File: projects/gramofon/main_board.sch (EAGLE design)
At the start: 25 parts

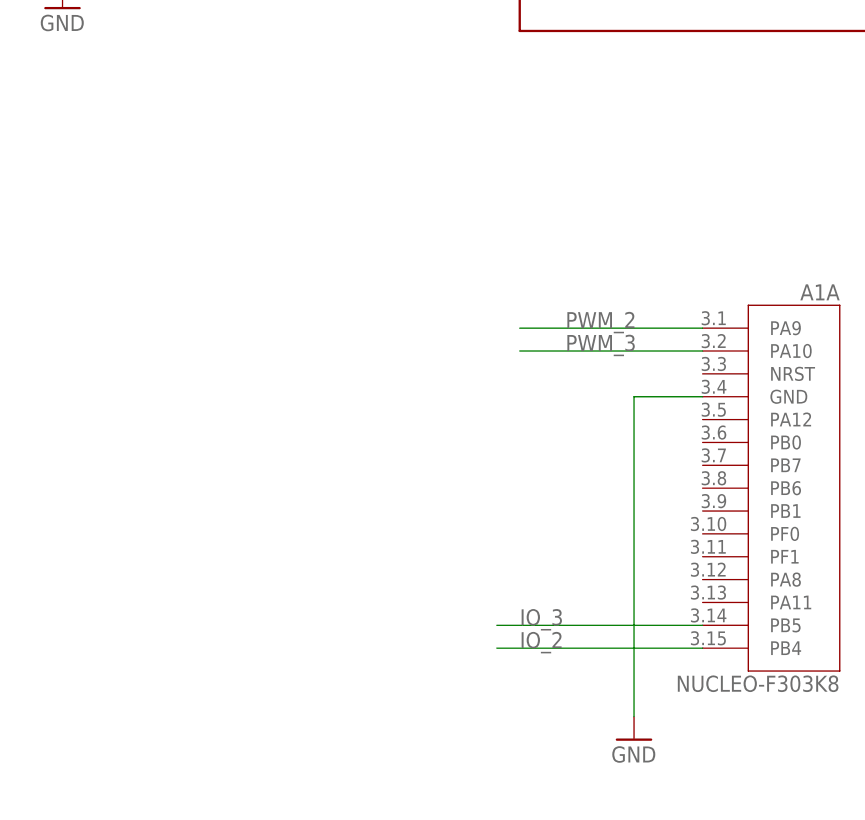
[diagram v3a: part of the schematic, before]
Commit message: updated battery board
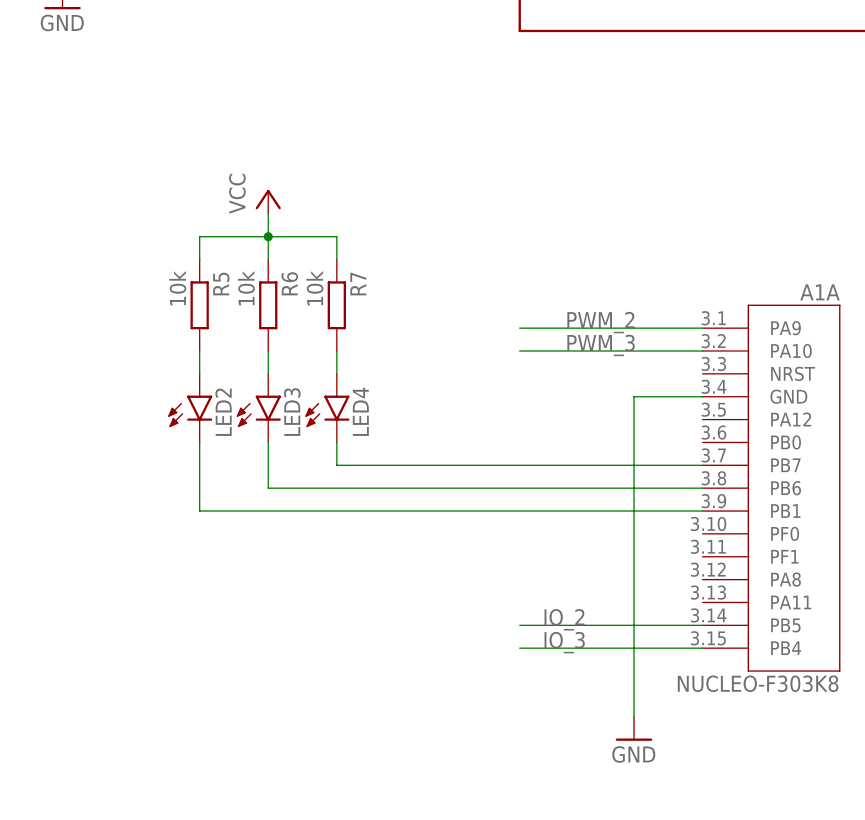
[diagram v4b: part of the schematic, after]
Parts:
- added LED2, LED3, LED4: (no value), led:LEDCHIPLED_1206
- added R5, R6, R7: 10k, rcl:R-EU_R1206
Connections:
- new net N$11: LED4.A, R7.2
- new net N$12: LED3.A, R6.2
- new net N$13: LED2.A, R5.2
- new net N$2: A1A.PB1, LED2.C
- new net N$3: A1A.PB6, LED3.C
- new net N$4: A1A.PB7, LED4.C
- net IO_2: now also A1A.PB5; no longer A1A.PB4
- net IO_3: now also A1A.PB4; no longer A1A.PB5
- net VCC: now also R5.1, R6.1, R7.1
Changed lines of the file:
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@@
 <part name="X10" library="con-wago-500" library_urn="urn:adsk.eagle:library:195" deviceset="W237-102" device="" package3d_urn="urn:adsk.eagle:package:10688/1"/>
 <part name="X11" library="con-wago-500" library_urn="urn:adsk.eagle:library:195" deviceset="W237-102" device="" package3d_urn="urn:adsk.eagle:package:10688/1"/>
+<part name="LED2" library="led" library_urn="urn:adsk.eagle:library:259" deviceset="LED" device="CHIPLED_1206" package3d_urn="urn:adsk.eagle:package:15823/2"/>
+<part name="LED3" library="led" library_urn="urn:adsk.eagle:library:259" deviceset="LED" device="CHIPLED_1206" package3d_urn="urn:adsk.eagle:package:15823/2"/>
+<part name="LED4" library="led" library_urn="urn:adsk.eagle:library:259" deviceset="LED" device="CHIPLED_1206" package3d_urn="urn:adsk.eagle:package:15823/2"/>
+<part name="R5" library="rcl" library_urn="urn:adsk.eagle:library:334" deviceset="R-EU_" device="R1206" package3d_urn="urn:adsk.eagle:package:23540/2" value="10k"/>
+<part name="R6" library="rcl" library_urn="urn:adsk.eagle:library:334" deviceset="R-EU_" device="R1206" package3d_urn="urn:adsk.eagle:package:23540/2" value="10k"/>
+<part name="R7" library="rcl" library_urn="urn:adsk.eagle:library:334" deviceset="R-EU_" device="R1206" package3d_urn="urn:adsk.eagle:package:23540/2" value="10k"/>
+<part name="P+5" library="supply1" library_urn="urn:adsk.eagle:library:371" deviceset="VCC" device=""/>
 </parts>
 <sheets>
@@
 <attribute name="VALUE" x="127" y="67.183" size="1.778" layer="96" rot="R180"/>
 <attribute name="NAME" x="124.46" y="62.611" size="1.778" layer="95"/>
+</instance>
+<instance part="LED2" gate="G$1" x="-30.48" y="78.74" smashed="yes">
+<attribute name="NAME" x="-26.924" y="74.168" size="1.778" layer="95" rot="R90"/>
+<attribute name="VALUE" x="-24.765" y="74.168" size="1.778" layer="96" rot="R90"/>
+</instance>
+<instance part="LED3" gate="G$1" x="-22.86" y="78.74" smashed="yes">
+<attribute name="NAME" x="-19.304" y="74.168" size="1.778" layer="95" rot="R90"/>
+<attribute name="VALUE" x="-17.145" y="74.168" size="1.778" layer="96" rot="R90"/>
+</instance>
+<instance part="LED4" gate="G$1" x="-15.24" y="78.74" smashed="yes">
+<attribute name="NAME" x="-11.684" y="74.168" size="1.778" layer="95" rot="R90"/>
+<attribute name="VALUE" x="-9.525" y="74.168" size="1.778" layer="96" rot="R90"/>
+</instance>
+<instance part="R5" gate="G$1" x="-30.48" y="88.9" smashed="yes" rot="R270">
+<attribute name="NAME" x="-28.9814" y="92.71" size="1.778" layer="95" rot="R270"/>
+<attribute name="VALUE" x="-33.782" y="92.71" size="1.778" layer="96" rot="R270"/>
+</instance>
+<instance part="R6" gate="G$1" x="-22.86" y="88.9" smashed="yes" rot="R270">
+<attribute name="NAME" x="-21.3614" y="92.71" size="1.778" layer="95" rot="R270"/>
+<attribute name="VALUE" x="-26.162" y="92.71" size="1.778" layer="96" rot="R270"/>
+</instance>
+<instance part="R7" gate="G$1" x="-15.24" y="88.9" smashed="yes" rot="R270">
+<attribute name="NAME" x="-13.7414" y="92.71" size="1.778" layer="95" rot="R270"/>
+<attribute name="VALUE" x="-18.542" y="92.71" size="1.778" layer="96" rot="R270"/>
+</instance>
+<instance part="P+5" gate="VCC" x="-22.86" y="101.6" smashed="yes">
+<attribute name="VALUE" x="-25.4" y="99.06" size="1.778" layer="96" rot="R90"/>
 </instance>
 </instances>
@@
 <wire x1="-38.1" y1="152.4" x2="-38.1" y2="149.86" width="0.1524" layer="91"/>
 <junction x="-38.1" y="149.86"/>
+</segment>
+<segment>
+<pinref part="R5" gate="G$1" pin="1"/>
+<wire x1="-30.48" y1="93.98" x2="-30.48" y2="96.52" width="0.1524" layer="91"/>
+<wire x1="-30.48" y1="96.52" x2="-22.86" y2="96.52" width="0.1524" layer="91"/>
+<pinref part="R7" gate="G$1" pin="1"/>
+<wire x1="-22.86" y1="96.52" x2="-15.24" y2="96.52" width="0.1524" layer="91"/>
+<wire x1="-15.24" y1="96.52" x2="-15.24" y2="93.98" width="0.1524" layer="91"/>
+<pinref part="R6" gate="G$1" pin="1"/>
+<wire x1="-22.86" y1="93.98" x2="-22.86" y2="96.52" width="0.1524" layer="91"/>
+<junction x="-22.86" y="96.52"/>
+<wire x1="-22.86" y1="96.52" x2="-22.86" y2="99.06" width="0.1524" layer="91"/>
+<pinref part="P+5" gate="VCC" pin="VCC"/>
 </segment>
 </net>
@@
 </segment>
 <segment>
-<pinref part="A1" gate="A" pin="PB4"/>
-<wire x1="25.4" y1="50.8" x2="2.54" y2="50.8" width="0.1524" layer="91"/>
-<label x="5.08" y="50.8" size="1.778" layer="95"/>
+<pinref part="A1" gate="A" pin="PB5"/>
+<wire x1="25.4" y1="53.34" x2="5.08" y2="53.34" width="0.1524" layer="91"/>
+<label x="7.62" y="53.34" size="1.778" layer="95"/>
 </segment>
 </net>
@@
 </segment>
 <segment>
-<pinref part="A1" gate="A" pin="PB5"/>
-<wire x1="25.4" y1="53.34" x2="2.54" y2="53.34" width="0.1524" layer="91"/>
-<label x="5.08" y="53.34" size="1.778" layer="95"/>
+<pinref part="A1" gate="A" pin="PB4"/>
+<wire x1="25.4" y1="50.8" x2="5.08" y2="50.8" width="0.1524" layer="91"/>
+<label x="7.62" y="50.8" size="1.778" layer="95"/>
 </segment>
 </net>
@@
 </segment>
 </net>
+<net name="N$2" class="0">
+<segment>
+<pinref part="A1" gate="A" pin="PB1"/>
+<pinref part="LED2" gate="G$1" pin="C"/>
+<wire x1="25.4" y1="66.04" x2="-30.48" y2="66.04" width="0.1524" layer="91"/>
+<wire x1="-30.48" y1="66.04" x2="-30.48" y2="73.66" width="0.1524" layer="91"/>
+</segment>
+</net>
+<net name="N$3" class="0">
+<segment>
+<pinref part="A1" gate="A" pin="PB6"/>
+<pinref part="LED3" gate="G$1" pin="C"/>
+<wire x1="25.4" y1="68.58" x2="-22.86" y2="68.58" width="0.1524" layer="91"/>
+<wire x1="-22.86" y1="68.58" x2="-22.86" y2="73.66" width="0.1524" layer="91"/>
+</segment>
+</net>
+<net name="N$4" class="0">
+<segment>
+<pinref part="A1" gate="A" pin="PB7"/>
+<pinref part="LED4" gate="G$1" pin="C"/>
+<wire x1="25.4" y1="71.12" x2="-15.24" y2="71.12" width="0.1524" layer="91"/>
+<wire x1="-15.24" y1="71.12" x2="-15.24" y2="73.66" width="0.1524" layer="91"/>
+</segment>
+</net>
+<net name="N$11" class="0">
+<segment>
+<pinref part="LED4" gate="G$1" pin="A"/>
+<pinref part="R7" gate="G$1" pin="2"/>
+<wire x1="-15.24" y1="81.28" x2="-15.24" y2="83.82" width="0.1524" layer="91"/>
+</segment>
+</net>
+<net name="N$12" class="0">
+<segment>
+<pinref part="LED3" gate="G$1" pin="A"/>
+<pinref part="R6" gate="G$1" pin="2"/>
+<wire x1="-22.86" y1="81.28" x2="-22.86" y2="83.82" width="0.1524" layer="91"/>
+</segment>
+</net>
+<net name="N$13" class="0">
+<segment>
+<pinref part="LED2" gate="G$1" pin="A"/>
+<pinref part="R5" gate="G$1" pin="2"/>
+<wire x1="-30.48" y1="81.28" x2="-30.48" y2="83.82" width="0.1524" layer="91"/>
+</segment>
+</net>
